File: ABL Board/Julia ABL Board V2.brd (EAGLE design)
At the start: 62.2 x 50.8 mm, 33 parts, among them Q2 MMBT4403, U1 HX711, U2 LM317, X1 LOADCELL 3, X2 LOADCELL 2, X4 INPUT, X5 LOADCELL, X9 ABL_LED

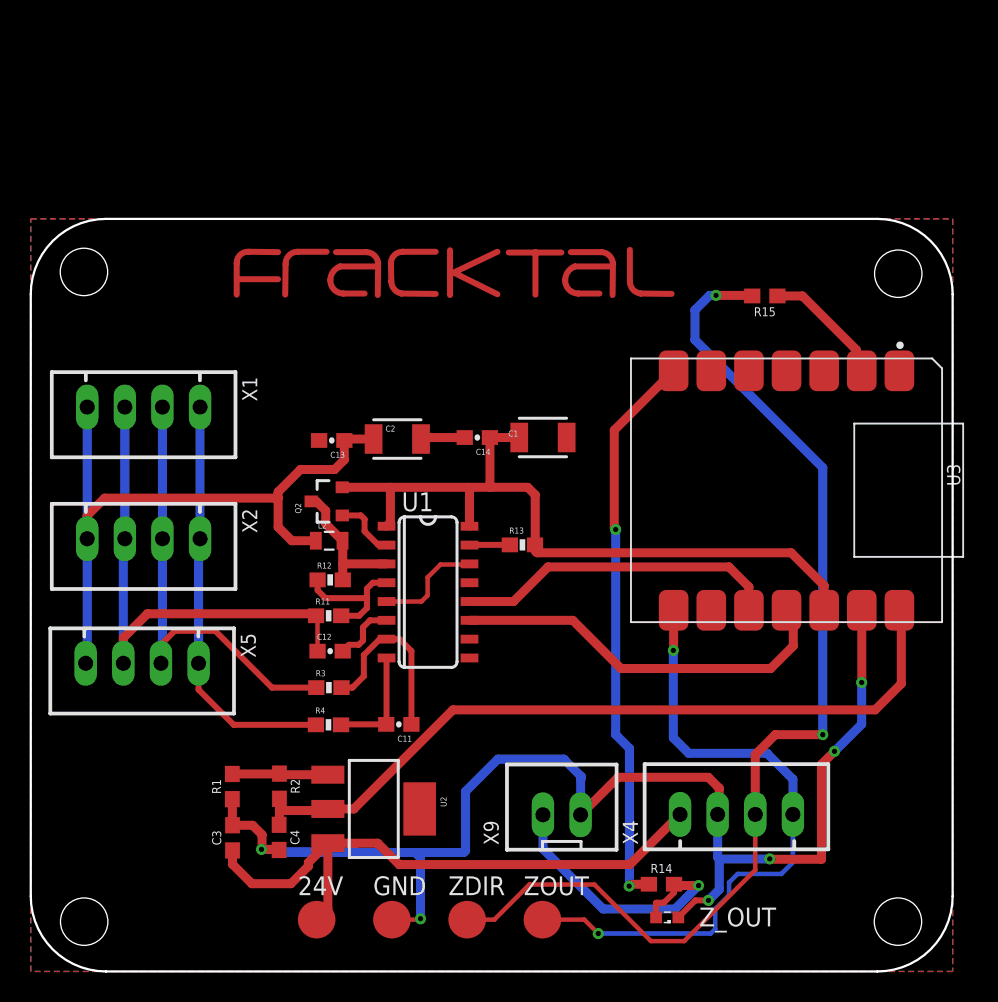
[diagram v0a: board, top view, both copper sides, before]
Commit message: Updated ABL V2 design, added Gerber, BOM and Centroids of V2
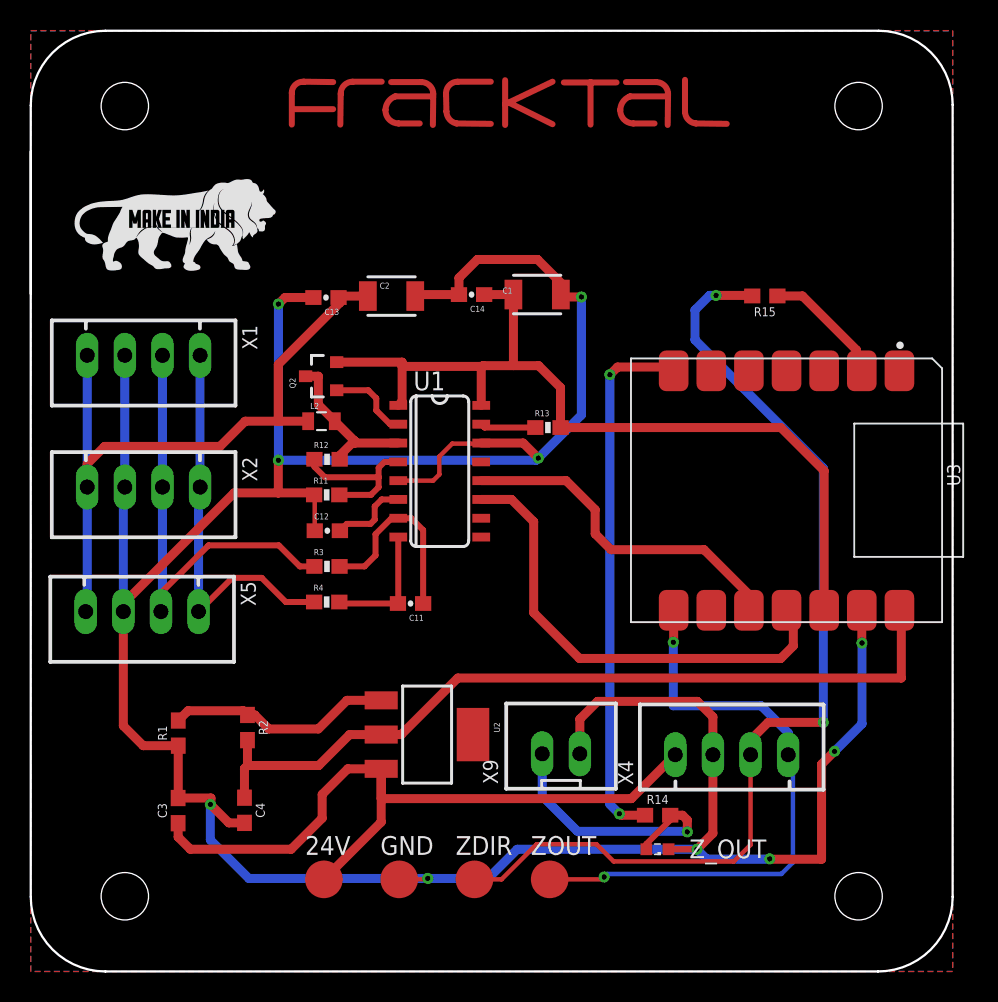
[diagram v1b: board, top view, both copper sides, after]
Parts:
- added U$1: (no value), FracktalWorks_Eagle_Library:MAKEININDIA
- moved U$2 12.1 mm to (80.4, 87.5)
- moved C1 9.66 mm to (85.0, 76.2)
- moved C14 9.66 mm to (80.6, 76.2)
- moved C2 9.66 mm to (75.2, 76.1)
- moved C13 9.66 mm to (70.7, 76.0)
- moved Q2 8.46 mm to (70.5, 70.7)
- moved R4 8.29 mm to (70.8, 55.4)
- moved U1 8.20 mm to (78.4, 64.2)
- moved C11 8.20 mm to (76.4, 55.3)
- moved R3 8.18 mm to (70.8, 57.8)
- moved R11 8.16 mm to (70.8, 62.7)
- moved R12 8.14 mm to (70.8, 65.1)
- moved C12 8.13 mm to (70.8, 60.2)
- moved R13 8.10 mm to (85.7, 67.2)
- moved L2 8.09 mm to (70.4, 67.6)
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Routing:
- net GND: track 141.6 -> 217.9 mm, vias 6 -> 10
- net 24V: track 40.4 -> 50.3 mm
- net 3.3V: track 49.9 -> 59.3 mm
- net ADJ: track 6.50 -> 15.3 mm
- net SCK: track 26.4 -> 32.1 mm
- net Z_DIR: track 73.4 -> 68.8 mm
- net Z_OUT: track 44.1 -> 40.8 mm
- net 5V: track 52.3 -> 55.2 mm
- net N$18: track 38.3 -> 36.3 mm
- net N$10: track 9.00 -> 10.8 mm
- net N$12: track 9.35 -> 11.0 mm
- net DAT: track 22.0 -> 23.3 mm
- net N$9: track 4.29 -> 5.58 mm
- net A+: track 28.0 -> 26.8 mm
- net N$17: track 19.9 -> 18.7 mm
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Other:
- board size 62.2 x 50.8 mm -> 62.2 x 63.5 mm
